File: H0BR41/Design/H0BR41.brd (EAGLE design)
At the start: 34.6 x 30 mm, 26 parts, among them P1 HEXABIT_17.32, U1 STM32G0B1CEU6NUFQFPN48_STM32_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, U2 LSM6DS3TR-C, U3 STMICROELECTRONICS_LSM303AGRT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, X1 8MH

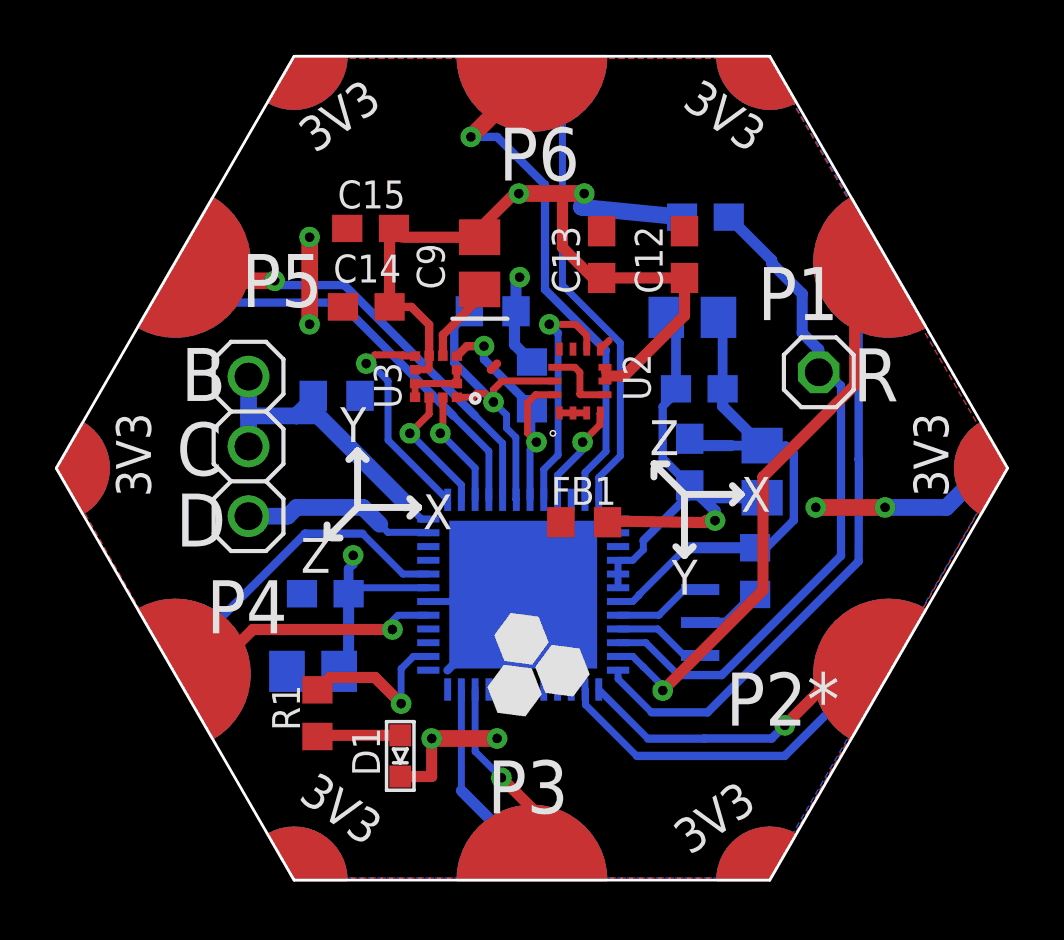
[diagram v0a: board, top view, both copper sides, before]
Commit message: -Changing the layout to be like of master design in terms of the position of sensors ICs . -Changing the Schematic as well
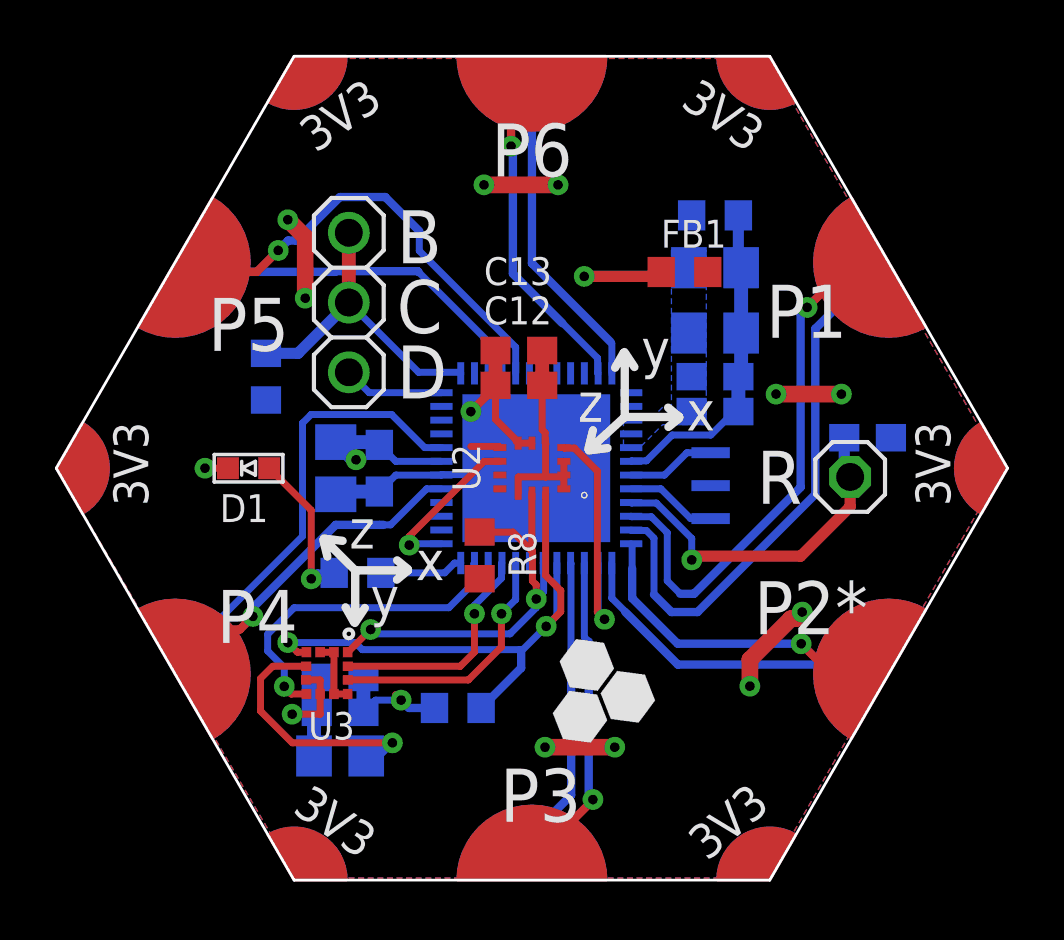
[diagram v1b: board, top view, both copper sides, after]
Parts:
- X1: value 8MH -> CSTNE8M00G550000R0
- moved C9 18.6 mm to (27.6, 23.7), flipped to the bottom, turned to 0 degrees
- moved C15 17.7 mm to (27.6, 25.2), flipped to the bottom
- moved R9 14.5 mm to (31.9, 25.4), turned to 180 degrees
- moved C14 13.5 mm to (27.6, 26.5), flipped to the bottom
- moved R3 13.0 mm to (41.3, 43.3), turned to 180 degrees
- moved D1 11.8 mm to (24.3, 34.1), turned to 270 degrees
- moved U3 11.5 mm to (27.1, 26.7), turned to 270 degrees
- moved C4 9.97 mm to (46.8, 35.2), turned to 0 degrees
- moved FB1 9.82 mm to (40.2, 41.3), turned to 180 degrees
- moved C12 7.69 mm to (34.1, 37.1), turned to 0 degrees
- moved C6 7.44 mm to (27.5, 34.1), turned to 270 degrees
- moved R8 6.48 mm to (32.7, 31.0), flipped to the top, turned to 90 degrees
- moved JP1 6.39 mm to (27.9, 40.2)
- moved C3 5.33 mm to (41.3, 39.1), turned to 180 degrees
- moved R1 5.32 mm to (28.3, 30.3), flipped to the bottom, turned to 0 degrees
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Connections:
- removed net N$17: R1.2, U1.26
- removed net N$19: D1.A, R1.1
- removed net N$2 (its old number): U1.9, X1.P$1
- new net N$1: R1.1, U1.24
- new net N$4: D1.A, R1.2
- new net N$5: U1.7, X1.P$1
- net C: now also U1.37; no longer U1.36
- net D: now also U1.36; no longer U1.35
- net GND: now also U1.42, U1.43, U1.44; no longer U1.1, U1.2, U1.24, U1.25
- net GND1: now also U1.6; no longer U1.7
- net IMU_INT1: now also U1.14; no longer U1.45
- net IMU_INT2: now also U1.25; no longer U1.44
- net MAG_INT: now also U1.23; no longer U1.37
- net R: now also U1.9; no longer U1.10
- net SCL: now also R8.2, U1.18; no longer R9.2, U1.42
- net SDA: now also R9.2, U1.17; no longer R8.2, U1.43
- net USART2_RX: now also U1.13; no longer U1.14
- net USART2_TX: now also U1.12; no longer U1.13
- net USART3_RX: now also P1.PAD_PD6, U1.48; no longer P1.PAD_PD3, U1.23
- net USART3_TX: now also P1.PAD_PU6, U1.47; no longer P1.PAD_PU3, U1.22
- net USART4_RX: now also U1.11; no longer U1.12
- net USART4_TX: now also U1.10; no longer U1.11
- net USART6_RX: now also P1.PAD_PD3, U1.16; no longer P1.PAD_PD6, U1.48
- net USART6_TX: now also P1.PAD_PU3, U1.15; no longer P1.PAD_PU6, U1.47
- net VCC: now also U1.3; no longer U1.6
- net XL_INT1: now also U1.21; no longer U1.39
- net XL_INT2: now also U1.20; no longer U1.38
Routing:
- net GND: track 53.7 -> 35.0 mm, vias 8 -> 13
- net VCC: track 20.5 -> 6.81 mm
- net R: track 24.6 -> 12.7 mm, vias 0 -> 1
- net SDA: track 10.3 -> 21.2 mm
- net GND1: track 19.4 -> 11.9 mm
- net USART6_TX: track 19.3 -> 11.9 mm
- net N$2: track 2.97 -> 9.46 mm, vias 0 -> 1
- net N$17: track 6.08 -> 0.00 mm, vias 1 -> 0
- net USART6_RX: track 17.1 -> 11.5 mm
- net N$4: track 0.00 -> 5.59 mm, vias 0 -> 1
- net IMU_INT1: track 3.81 -> 9.22 mm
- net USART3_TX: track 7.11 -> 12.5 mm
- net USART3_RX: track 7.32 -> 12.1 mm
- net USART1_RX: track 11.6 -> 16.2 mm
- net XL_INT2: track 4.79 -> 9.36 mm
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- added copper zone on layer 16, net VCC
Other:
- board text added: "x"
- board text added: "y"
- board text added: "z"
- board text removed: "X"
- board text removed: "Y"
- board text removed: "Z"

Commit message: -Correcting some fault connections
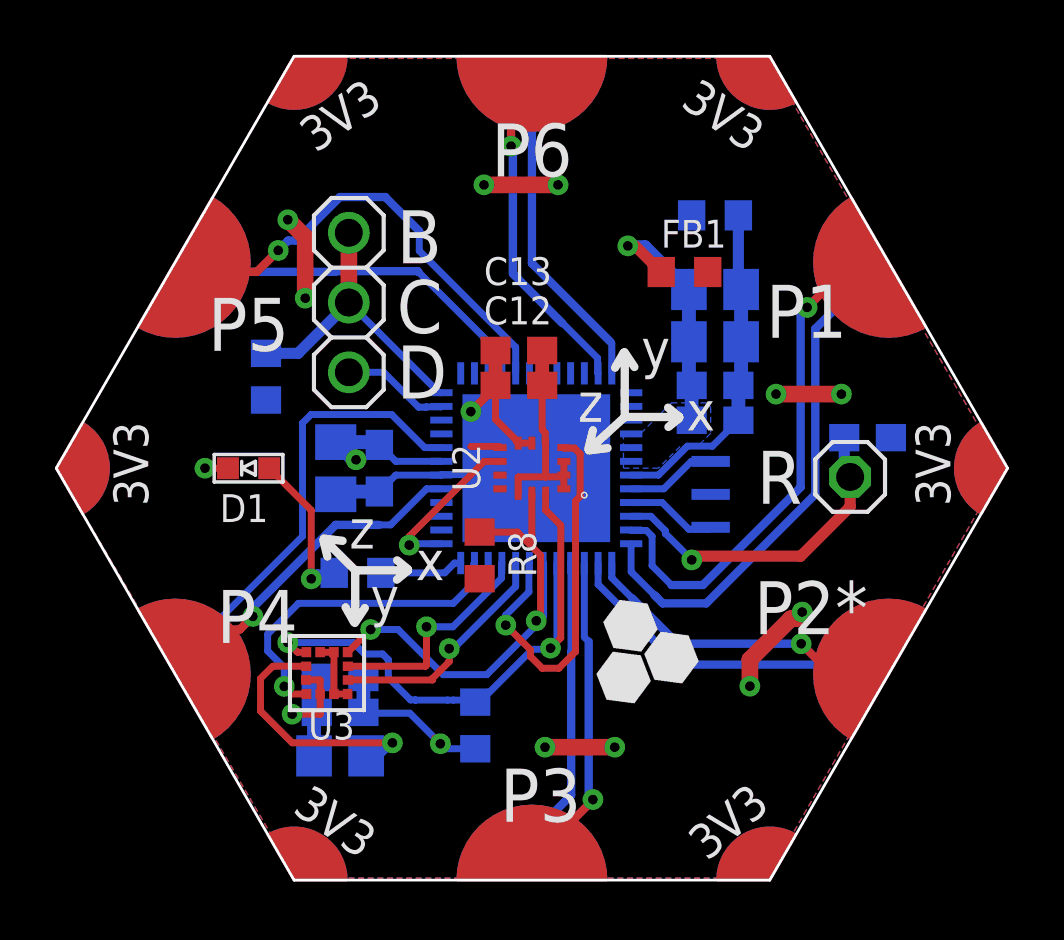
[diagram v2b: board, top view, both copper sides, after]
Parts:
- moved R9 0.90 mm to (32.5, 24.8), turned to 90 degrees
- moved C8 0.79 mm to (41.3, 40.6)
- moved C1 0.32 mm to (41.3, 35.9)
- moved C3 0.32 mm to (41.3, 38.7)
- moved C7 0.32 mm to (41.3, 37.1)
- moved X1 0.32 mm to (41.1, 33.2)
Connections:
- net C: now also U1.36; no longer U1.37
- net D: now also U1.35; no longer U1.36
- net GND1: now also U1.7; no longer U1.6
- net IMU_INT1: now also U1.19; no longer U1.14
- net N$3: now also U1.9; no longer U1.8
- net N$5: now also U1.8; no longer U1.7
- net R: now also U1.10; no longer U1.9
- net USART2_RX: now also U1.14; no longer U1.13
- net USART2_TX: now also U1.13; no longer U1.12
- net USART4_RX: now also U1.12; no longer U1.11
- net USART4_TX: now also U1.11; no longer U1.10
- net VCC: now also U1.6; no longer U1.3
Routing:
- net IMU_INT1: track 9.22 -> 14.2 mm
- net VCC: track 6.81 -> 9.29 mm
- net SCL: track 15.7 -> 18.0 mm
- net VDD: track 21.3 -> 23.0 mm
- net USART4_RX: track 19.9 -> 18.9 mm
- net USART4_TX: track 19.5 -> 18.7 mm
- net XL_INT2: track 9.36 -> 8.71 mm
- net SDA: track 21.2 -> 21.8 mm
- net R: track 12.7 -> 12.1 mm
- net GND1: track 11.9 -> 12.4 mm

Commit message: -Correcting some issues related to part names
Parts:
- removed C15, C5: 100nF, HEXABITZ_RCLS:C-0603
- removed C9: 220nF, HEXABITZ_RCLS:C-0805-POL
- added C10, C11: 100nF, HEXABITZ_RCLS:C-0603
- added C2: 1uF, HEXABITZ_RCLS:C-0805-POL
- C14: value 100nF -> 220nF; device HEXABITZ_RCLS:C-0603 -> HEXABITZ_RCLS:C-0805-POL
- C4: value 100nF -> 4.7uF; device HEXABITZ_RCLS:C-0603 -> HEXABITZ_RCLS:C-0805-POL
- C6: value 4.7uF -> 100nF; device HEXABITZ_RCLS:C-0805-POL -> HEXABITZ_RCLS:C-0603
- C8: value 1uF -> 100nF; device HEXABITZ_RCLS:C-0805-POL -> HEXABITZ_RCLS:C-0603
- moved C4 19.4 mm to (27.5, 34.1), turned to 270 degrees
- moved C13 14.7 mm to (27.6, 25.2), flipped to the bottom, turned to 180 degrees
- moved C6 13.9 mm to (41.3, 35.9), turned to 0 degrees
- moved C8 13.8 mm to (29.1, 34.1), turned to 90 degrees
- moved C12 12.5 mm to (27.6, 26.5), flipped to the bottom, turned to 180 degrees
- moved C1 5.59 mm to (46.8, 35.2)
- moved C14 2.86 mm to (27.6, 23.7), turned to 0 degrees
- renumbered R8 to R5, R9 to R4
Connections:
- net GND: now also C1.1, C10.1, C11.1, C14.2, C4.2, C8.1; no longer C14.1, C15.1, C4.1, C5.1, C6.2, C9.2
- net GND1: now also C2.2, C6.1; no longer C1.1, C8.2
- net N$2: now also C14.1; no longer C9.1
- net R: now also C1.2; no longer C4.2
- net VCC: now also C2.1, C6.2; no longer C1.2, C8.1
- net VDD: now also C10.2, C11.2, C4.1, C8.2; no longer C14.2, C15.2, C5.2, C6.1
